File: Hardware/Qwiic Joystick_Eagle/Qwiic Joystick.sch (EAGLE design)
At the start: 26 parts, among them J1 Qwiic Right Angle, J4 Qwiic Right Angle, J6 AVR_SPI_PROG_3X2TESTPOINTS, U1 ATTIN85_SOIC_5.3MM

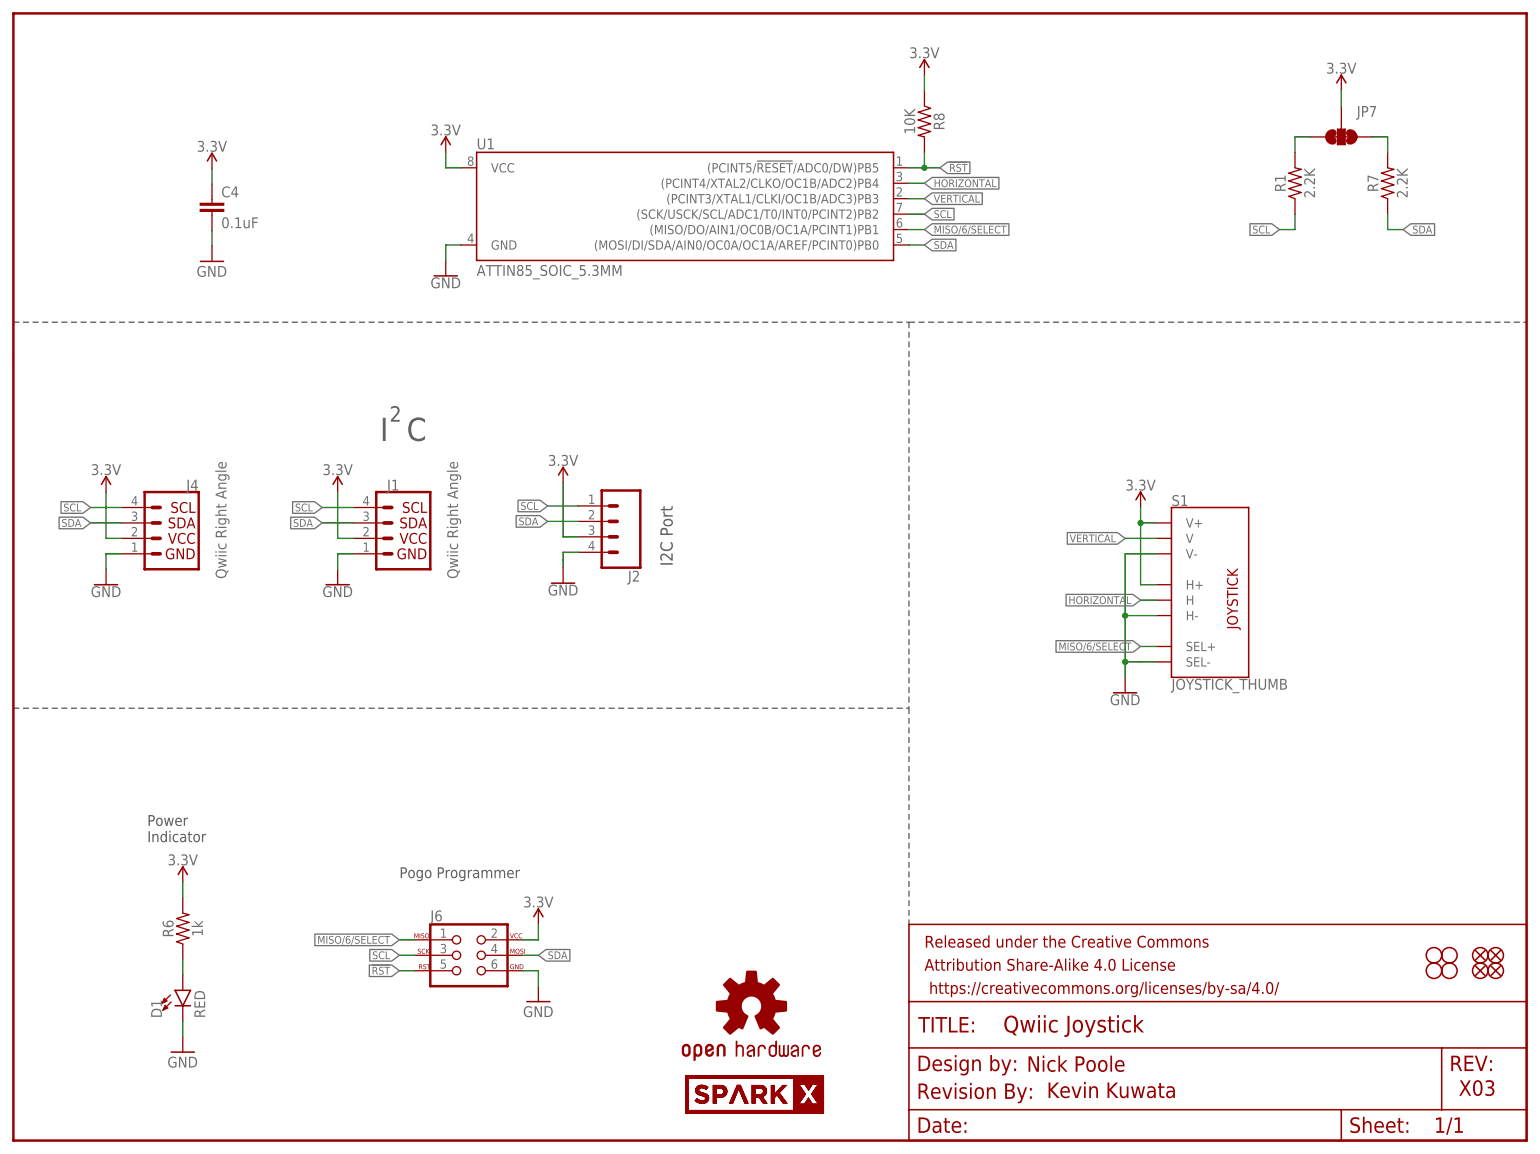
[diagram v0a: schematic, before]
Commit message: Cleaned repo
Cleaned up the repo, made parts sparkle parts.
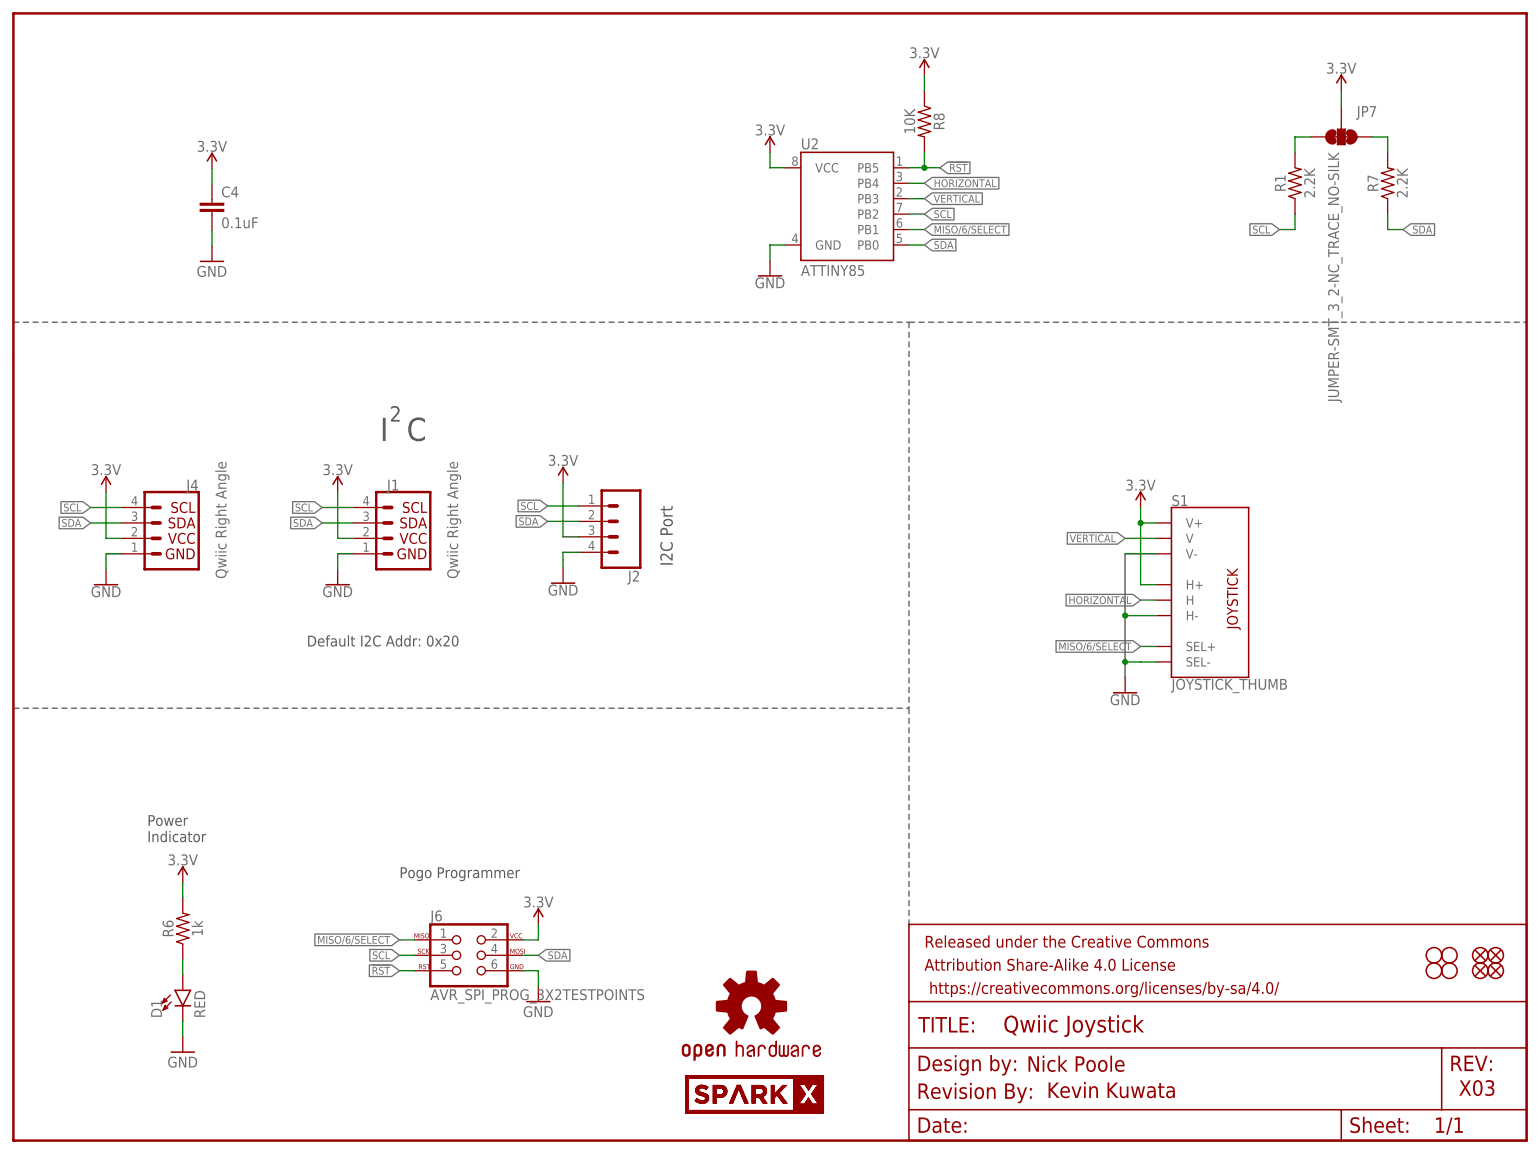
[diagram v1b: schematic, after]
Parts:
- removed U1: ATTIN85_SOIC_5.3MM, attiny85:ATTIN85_SOIC_5.3MM
- added U2: ATTINY85, SparkFun-IC-Microcontroller:ATTINY85
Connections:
- net !RST: now also U2.PB5; no longer U1.(PCINT5/!RESET!/ADC0/DW)PB5
- net 3.3V: now also U2.VCC; no longer U1.VCC
- net GND: now also U2.GND; no longer U1.GND
- net HORIZONTAL: now also U2.PB4; no longer U1.(PCINT4/XTAL2/CLKO/OC1B/ADC2)PB4
- net MISO/6/SELECT: now also U2.PB1; no longer U1.(MISO/DO/AIN1/OC0B/OC1A/PCINT1)PB1
- net SCL: now also U2.PB2; no longer U1.(SCK/USCK/SCL/ADC1/T0/INT0/PCINT2)PB2
- net SDA: now also U2.PB0; no longer U1.(MOSI/DI/SDA/AIN0/OC0A/OC1A/AREF/PCINT0)PB0
- net VERTICAL: now also U2.PB3; no longer U1.(PCINT3/XTAL1/CLKI/OC1B/ADC3)PB3
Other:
- note added: "Default I2C Addr: 0x20"
